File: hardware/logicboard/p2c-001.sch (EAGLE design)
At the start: 47 parts, among them IC1 74LS07N, K1 G5V1, T1 2SC1815

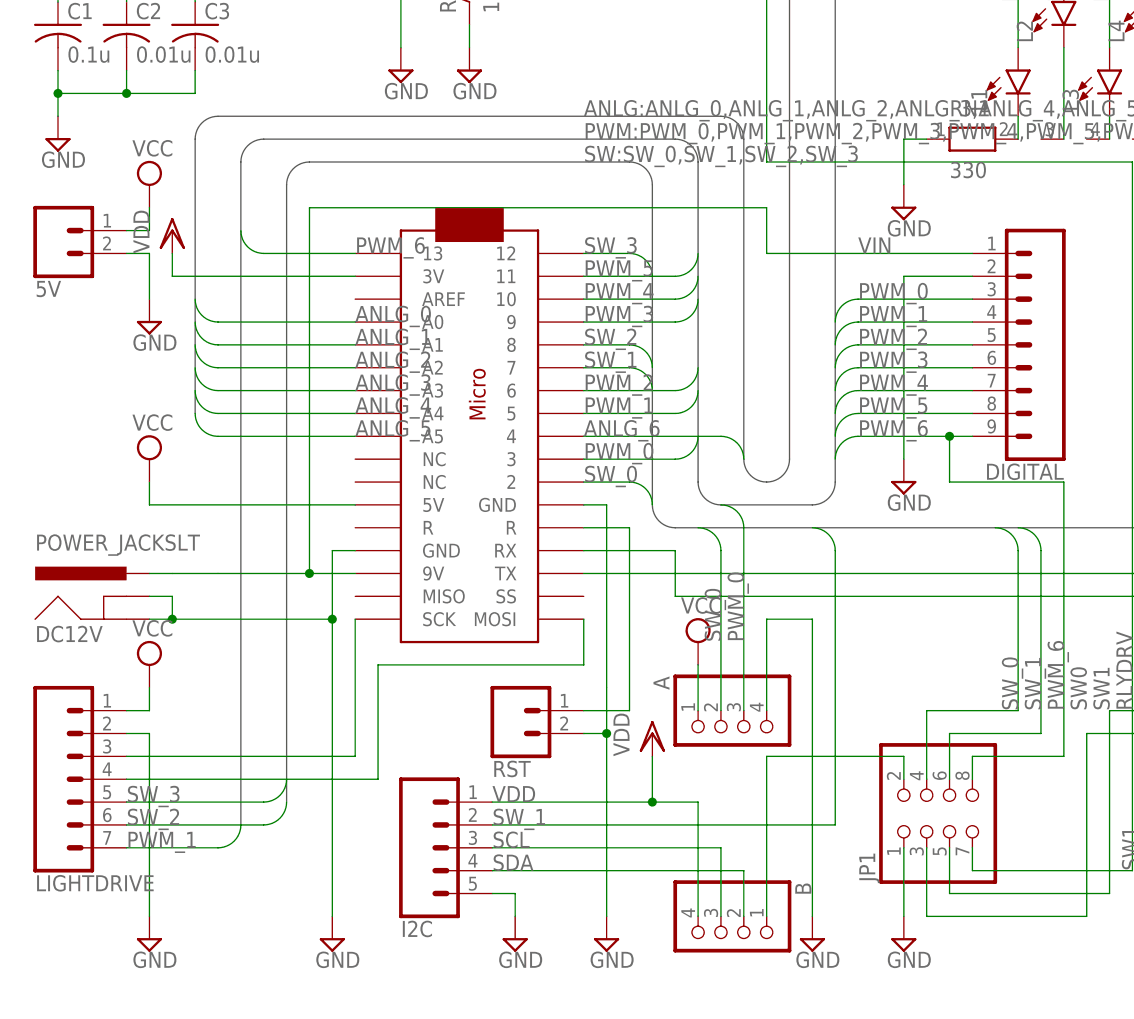
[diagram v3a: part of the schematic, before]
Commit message: Reversed Digital pin.
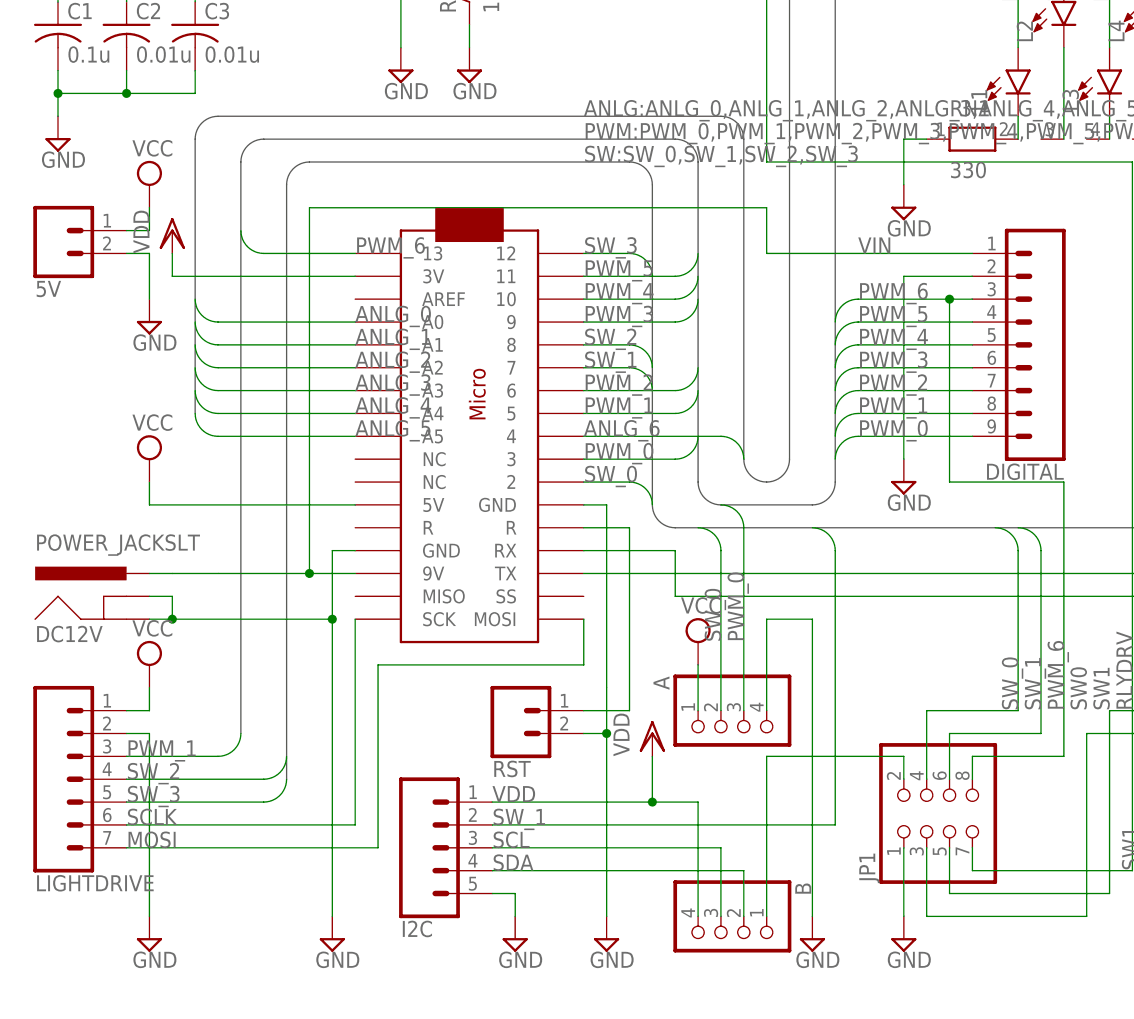
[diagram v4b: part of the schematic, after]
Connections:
- removed net SCK: LIGHTDRIVE.3, U$2.SCK
- new net SCLK: LIGHTDRIVE.6, U$2.SCK
- net MOSI: now also LIGHTDRIVE.7; no longer LIGHTDRIVE.4
- net PWM_0: now also DIGITAL.9; no longer DIGITAL.3
- net PWM_1: now also DIGITAL.8, LIGHTDRIVE.3; no longer DIGITAL.4, LIGHTDRIVE.7
- net PWM_2: now also DIGITAL.7; no longer DIGITAL.5
- net PWM_4: now also DIGITAL.5; no longer DIGITAL.7
- net PWM_5: now also DIGITAL.4; no longer DIGITAL.8
- net PWM_6: now also DIGITAL.3; no longer DIGITAL.9
- net SW_2: now also LIGHTDRIVE.4; no longer LIGHTDRIVE.6
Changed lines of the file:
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@@
 <setting verticaltext="up"/>
 </settings>
-<grid distance="0.1" unitdist="inch" unit="inch" style="lines" multiple="1" display="no" altdistance="0.01" altunitdist="inch" altunit="inch"/>
+<grid distance="0.1" unitdist="inch" unit="inch" style="dots" multiple="1" display="yes" altdistance="0.01" altunitdist="inch" altunit="inch"/>
 <layers>
 <layer number="1" name="Top" color="4" fill="1" visible="no" active="no"/>
@@
 <bus name="PWM:PWM_0,PWM_1,PWM_2,PWM_3,PWM_4,PWM_5,PWM_6">
 <segment>
-<wire x1="30.48" y1="27.94" x2="30.48" y2="101.6" width="0.762" layer="92"/>
+<wire x1="30.48" y1="38.1" x2="30.48" y2="101.6" width="0.762" layer="92"/>
 <wire x1="30.48" y1="101.6" x2="33.02" y2="104.14" width="0.762" layer="92" curve="-90"/>
 <wire x1="33.02" y1="104.14" x2="78.74" y2="104.14" width="0.762" layer="92"/>
@@
 <wire x1="73.66" y1="101.6" x2="38.1" y2="101.6" width="0.762" layer="92"/>
 <wire x1="38.1" y1="101.6" x2="35.56" y2="99.06" width="0.762" layer="92" curve="90"/>
-<wire x1="35.56" y1="99.06" x2="35.56" y2="30.48" width="0.762" layer="92"/>
+<wire x1="35.56" y1="99.06" x2="35.56" y2="33.02" width="0.762" layer="92"/>
 <label x="68.58" y="101.6" size="1.778" layer="95"/>
 </segment>
@@
 </segment>
 <segment>
-<pinref part="LIGHTDRIVE" gate="G$1" pin="6"/>
-<wire x1="35.56" y1="30.48" x2="33.02" y2="27.94" width="0.1524" layer="91" curve="-90"/>
-<wire x1="33.02" y1="27.94" x2="17.78" y2="27.94" width="0.1524" layer="91"/>
-<label x="17.78" y="27.94" size="1.778" layer="95"/>
+<pinref part="LIGHTDRIVE" gate="G$1" pin="4"/>
+<wire x1="35.56" y1="35.56" x2="33.02" y2="33.02" width="0.1524" layer="91" curve="-90"/>
+<wire x1="33.02" y1="33.02" x2="17.78" y2="33.02" width="0.1524" layer="91"/>
+<label x="17.78" y="33.02" size="1.778" layer="95"/>
 </segment>
 </net>
@@
 </segment>
 <segment>
-<wire x1="96.52" y1="68.58" x2="99.06" y2="71.12" width="0.1524" layer="91" curve="-90"/>
-<wire x1="99.06" y1="71.12" x2="109.22" y2="71.12" width="0.1524" layer="91"/>
-<label x="99.06" y="71.12" size="1.778" layer="95"/>
-<wire x1="109.22" y1="71.12" x2="111.76" y2="71.12" width="0.1524" layer="91"/>
-<wire x1="109.22" y1="71.12" x2="109.22" y2="66.04" width="0.1524" layer="91"/>
-<junction x="109.22" y="71.12"/>
+<pinref part="DIGITAL" gate="G$1" pin="3"/>
+<wire x1="96.52" y1="83.82" x2="99.06" y2="86.36" width="0.1524" layer="91" curve="-90"/>
+<wire x1="99.06" y1="86.36" x2="109.22" y2="86.36" width="0.1524" layer="91"/>
+<label x="99.06" y="86.36" size="1.778" layer="95"/>
+<wire x1="109.22" y1="86.36" x2="111.76" y2="86.36" width="0.1524" layer="91"/>
 <wire x1="109.22" y1="66.04" x2="121.92" y2="66.04" width="0.1524" layer="91"/>
 <wire x1="121.92" y1="66.04" x2="121.92" y2="35.56" width="0.1524" layer="91"/>
@@
 <wire x1="111.76" y1="35.56" x2="111.76" y2="33.02" width="0.1524" layer="91"/>
 <label x="121.92" y="40.64" size="1.778" layer="95" rot="R90"/>
-<pinref part="DIGITAL" gate="G$1" pin="9"/>
+<wire x1="109.22" y1="86.36" x2="109.22" y2="66.04" width="0.1524" layer="91"/>
+<junction x="109.22" y="86.36"/>
 </segment>
 </net>
@@
 </segment>
 <segment>
-<wire x1="96.52" y1="71.12" x2="99.06" y2="73.66" width="0.1524" layer="91" curve="-90"/>
-<wire x1="99.06" y1="73.66" x2="111.76" y2="73.66" width="0.1524" layer="91"/>
-<label x="99.06" y="73.66" size="1.778" layer="95"/>
-<pinref part="DIGITAL" gate="G$1" pin="8"/>
+<pinref part="DIGITAL" gate="G$1" pin="4"/>
+<wire x1="96.52" y1="81.28" x2="99.06" y2="83.82" width="0.1524" layer="91" curve="-90"/>
+<wire x1="99.06" y1="83.82" x2="111.76" y2="83.82" width="0.1524" layer="91"/>
+<label x="99.06" y="83.82" size="1.778" layer="95"/>
 </segment>
 </net>
@@
 </segment>
 <segment>
-<wire x1="96.52" y1="73.66" x2="99.06" y2="76.2" width="0.1524" layer="91" curve="-90"/>
-<wire x1="99.06" y1="76.2" x2="111.76" y2="76.2" width="0.1524" layer="91"/>
-<label x="99.06" y="76.2" size="1.778" layer="95"/>
-<pinref part="DIGITAL" gate="G$1" pin="7"/>
+<pinref part="DIGITAL" gate="G$1" pin="5"/>
+<wire x1="96.52" y1="78.74" x2="99.06" y2="81.28" width="0.1524" layer="91" curve="-90"/>
+<wire x1="99.06" y1="81.28" x2="111.76" y2="81.28" width="0.1524" layer="91"/>
+<label x="99.06" y="81.28" size="1.778" layer="95"/>
 </segment>
 </net>
@@
 </segment>
 <segment>
+<pinref part="DIGITAL" gate="G$1" pin="6"/>
 <wire x1="96.52" y1="76.2" x2="99.06" y2="78.74" width="0.1524" layer="91" curve="-90"/>
 <wire x1="99.06" y1="78.74" x2="111.76" y2="78.74" width="0.1524" layer="91"/>
 <label x="99.06" y="78.74" size="1.778" layer="95"/>
-<pinref part="DIGITAL" gate="G$1" pin="6"/>
 </segment>
 </net>
@@
 </segment>
 <segment>
-<wire x1="96.52" y1="83.82" x2="99.06" y2="86.36" width="0.1524" layer="91" curve="-90"/>
-<wire x1="99.06" y1="86.36" x2="111.76" y2="86.36" width="0.1524" layer="91"/>
-<label x="99.06" y="86.36" size="1.778" layer="95"/>
-<pinref part="DIGITAL" gate="G$1" pin="3"/>
-</segment>
-<segment>
 <pinref part="A" gate="A" pin="3"/>
 <wire x1="83.82" y1="63.5" x2="86.36" y2="60.96" width="0.1524" layer="91" curve="-90"/>
@@
 <label x="86.36" y="48.26" size="1.778" layer="95" rot="R90"/>
 </segment>
+<segment>
+<pinref part="DIGITAL" gate="G$1" pin="9"/>
+<wire x1="96.52" y1="68.58" x2="99.06" y2="71.12" width="0.1524" layer="91" curve="-90"/>
+<wire x1="99.06" y1="71.12" x2="111.76" y2="71.12" width="0.1524" layer="91"/>
+<label x="99.06" y="71.12" size="1.778" layer="95"/>
+</segment>
 </net>
 <net name="PWM_2" class="0">
@@
 </segment>
 <segment>
-<wire x1="96.52" y1="78.74" x2="99.06" y2="81.28" width="0.1524" layer="91" curve="-90"/>
-<wire x1="99.06" y1="81.28" x2="111.76" y2="81.28" width="0.1524" layer="91"/>
-<label x="99.06" y="81.28" size="1.778" layer="95"/>
-<pinref part="DIGITAL" gate="G$1" pin="5"/>
+<pinref part="DIGITAL" gate="G$1" pin="7"/>
+<wire x1="96.52" y1="73.66" x2="99.06" y2="76.2" width="0.1524" layer="91" curve="-90"/>
+<wire x1="99.06" y1="76.2" x2="111.76" y2="76.2" width="0.1524" layer="91"/>
+<label x="99.06" y="76.2" size="1.778" layer="95"/>
 </segment>
 </net>
@@
 </segment>
 <segment>
-<wire x1="96.52" y1="81.28" x2="99.06" y2="83.82" width="0.1524" layer="91" curve="-90"/>
-<wire x1="99.06" y1="83.82" x2="111.76" y2="83.82" width="0.1524" layer="91"/>
-<label x="99.06" y="83.82" size="1.778" layer="95"/>
-<pinref part="DIGITAL" gate="G$1" pin="4"/>
-</segment>
-<segment>
-<pinref part="LIGHTDRIVE" gate="G$1" pin="7"/>
-<wire x1="30.48" y1="27.94" x2="27.94" y2="25.4" width="0.1524" layer="91" curve="-90"/>
-<wire x1="27.94" y1="25.4" x2="17.78" y2="25.4" width="0.1524" layer="91"/>
-<label x="17.78" y="25.4" size="1.778" layer="95"/>
+<pinref part="LIGHTDRIVE" gate="G$1" pin="3"/>
+<wire x1="30.48" y1="38.1" x2="27.94" y2="35.56" width="0.1524" layer="91" curve="-90"/>
+<wire x1="27.94" y1="35.56" x2="17.78" y2="35.56" width="0.1524" layer="91"/>
+<label x="17.78" y="35.56" size="1.778" layer="95"/>
+</segment>
+<segment>
+<pinref part="DIGITAL" gate="G$1" pin="8"/>
+<wire x1="96.52" y1="71.12" x2="99.06" y2="73.66" width="0.1524" layer="91" curve="-90"/>
+<wire x1="99.06" y1="73.66" x2="111.76" y2="73.66" width="0.1524" layer="91"/>
+<label x="99.06" y="73.66" size="1.778" layer="95"/>
 </segment>
 </net>
@@
 </segment>
 </net>
-<net name="SCK" class="0">
-<segment>
-<pinref part="U$2" gate="G$1" pin="SCK"/>
-<wire x1="43.18" y1="50.8" x2="43.18" y2="35.56" width="0.1524" layer="91"/>
-<pinref part="LIGHTDRIVE" gate="G$1" pin="3"/>
-<wire x1="43.18" y1="35.56" x2="17.78" y2="35.56" width="0.1524" layer="91"/>
-</segment>
-</net>
 <net name="MOSI" class="0">
 <segment>
@@
 <wire x1="68.58" y1="50.8" x2="68.58" y2="45.72" width="0.1524" layer="91"/>
 <wire x1="68.58" y1="45.72" x2="45.72" y2="45.72" width="0.1524" layer="91"/>
-<wire x1="45.72" y1="45.72" x2="45.72" y2="33.02" width="0.1524" layer="91"/>
-<pinref part="LIGHTDRIVE" gate="G$1" pin="4"/>
-<wire x1="45.72" y1="33.02" x2="17.78" y2="33.02" width="0.1524" layer="91"/>
-</segment>
-</net>
+<wire x1="45.72" y1="45.72" x2="45.72" y2="25.4" width="0.1524" layer="91"/>
+<pinref part="LIGHTDRIVE" gate="G$1" pin="7"/>
+<wire x1="45.72" y1="25.4" x2="17.78" y2="25.4" width="0.1524" layer="91"/>
+<label x="17.78" y="25.4" size="1.778" layer="95"/>
+</segment>
+</net>
+<net name="SCLK" class="0">
+<segment>
+<pinref part="U$2" gate="G$1" pin="SCK"/>
+<wire x1="43.18" y1="50.8" x2="43.18" y2="27.94" width="0.1524" layer="91"/>
+<pinref part="LIGHTDRIVE" gate="G$1" pin="6"/>
+<wire x1="43.18" y1="27.94" x2="17.78" y2="27.94" width="0.1524" layer="91"/>
+<label x="17.78" y="27.94" size="1.778" layer="95"/>
+</segment>
+</net>

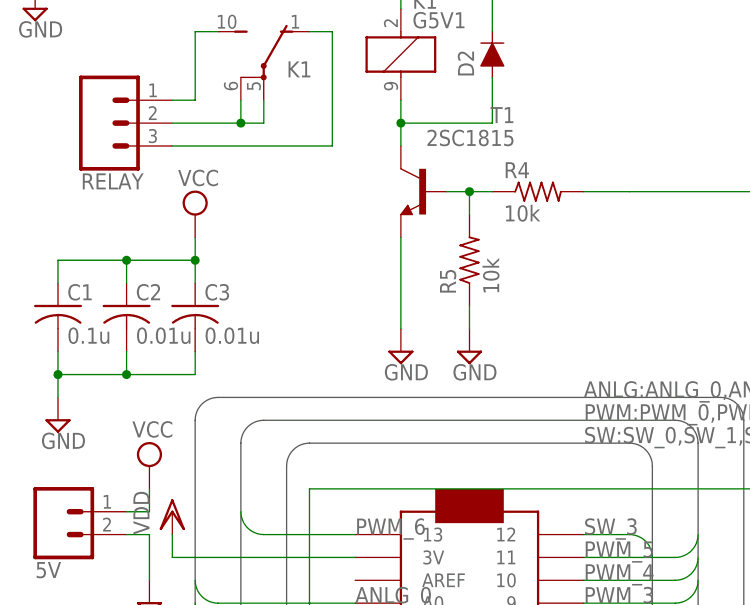
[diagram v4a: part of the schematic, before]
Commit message: Added I2C Rs.
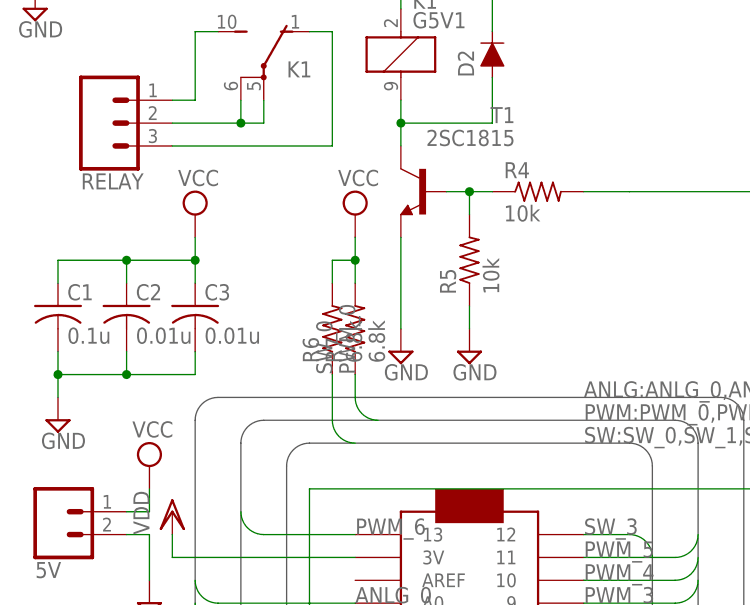
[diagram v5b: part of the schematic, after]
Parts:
- added R6, R7: 6.8k, resistor:R-US_0204/5
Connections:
- net PWM_0: now also R7.1
- net SW_0: now also R6.1
- net VCC: now also R6.2, R7.2
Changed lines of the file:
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@@
 <setting verticaltext="up"/>
 </settings>
-<grid distance="0.1" unitdist="inch" unit="inch" style="dots" multiple="1" display="yes" altdistance="0.01" altunitdist="inch" altunit="inch"/>
+<grid distance="0.1" unitdist="inch" unit="inch" style="lines" multiple="1" display="no" altdistance="0.01" altunitdist="inch" altunit="inch"/>
 <layers>
 <layer number="1" name="Top" color="4" fill="1" visible="no" active="no"/>
@@
 <part name="POGOPIN" library="pinhead" library_urn="urn:adsk.eagle:library:325" deviceset="PINHD-1X1" device="" package3d_urn="urn:adsk.eagle:package:22485/2"/>
 <part name="5V" library="SparkFun-Connectors" library_urn="urn:adsk.eagle:library:513" deviceset="CONN_02" device="" package3d_urn="urn:adsk.eagle:package:38039/1"/>
+<part name="SUPPLY26" library="supply2" library_urn="urn:adsk.eagle:library:372" deviceset="VCC" device=""/>
+<part name="R6" library="resistor" library_urn="urn:adsk.eagle:library:348" deviceset="R-US_" device="0204/5" package3d_urn="urn:adsk.eagle:package:25955/1" value="6.8k"/>
+<part name="R7" library="resistor" library_urn="urn:adsk.eagle:library:348" deviceset="R-US_" device="0204/5" package3d_urn="urn:adsk.eagle:package:25955/1" value="6.8k"/>
 </parts>
 <sheets>
@@
 <instance part="POGOPIN" gate="G$1" x="236.22" y="127"/>
 <instance part="5V" gate="G$1" x="10.16" y="93.98" rot="MR180"/>
+<instance part="SUPPLY26" gate="G$1" x="43.18" y="127"/>
+<instance part="R6" gate="G$1" x="40.64" y="114.3" rot="R90"/>
+<instance part="R7" gate="G$1" x="43.18" y="114.3" rot="R90"/>
 </instances>
 <busses>
@@
 <wire x1="20.32" y1="40.64" x2="17.78" y2="40.64" width="0.1524" layer="91"/>
 </segment>
+<segment>
+<pinref part="R6" gate="G$1" pin="2"/>
+<wire x1="40.64" y1="119.38" x2="40.64" y2="121.92" width="0.1524" layer="91"/>
+<wire x1="40.64" y1="121.92" x2="43.18" y2="121.92" width="0.1524" layer="91"/>
+<pinref part="R7" gate="G$1" pin="2"/>
+<wire x1="43.18" y1="121.92" x2="43.18" y2="119.38" width="0.1524" layer="91"/>
+<pinref part="SUPPLY26" gate="G$1" pin="VCC"/>
+<wire x1="43.18" y1="121.92" x2="43.18" y2="124.46" width="0.1524" layer="91"/>
+<junction x="43.18" y="121.92"/>
+</segment>
 </net>
 <net name="MIDIOUT-" class="0">
@@
 <label x="83.82" y="48.26" size="1.778" layer="95" rot="R90"/>
 </segment>
+<segment>
+<wire x1="43.18" y1="101.6" x2="40.64" y2="104.14" width="0.1524" layer="91" curve="-90"/>
+<wire x1="40.64" y1="104.14" x2="40.64" y2="109.22" width="0.1524" layer="91"/>
+<label x="40.64" y="109.22" size="1.778" layer="95" rot="R90"/>
+<pinref part="R6" gate="G$1" pin="1"/>
+</segment>
 </net>
 <net name="LED1K" class="0">
@@
 <label x="99.06" y="71.12" size="1.778" layer="95"/>
 </segment>
-</net>
+<segment>
+<wire x1="45.72" y1="104.14" x2="43.18" y2="106.68" width="0.1524" layer="91" curve="-90"/>
+<wire x1="43.18" y1="106.68" x2="43.18" y2="109.22" width="0.1524" layer="91"/>
+<label x="43.18" y="109.22" size="1.778" layer="95" rot="R90"/>
+<pinref part="R7" gate="G$1" pin="1"/>
+</segment>
+</net>

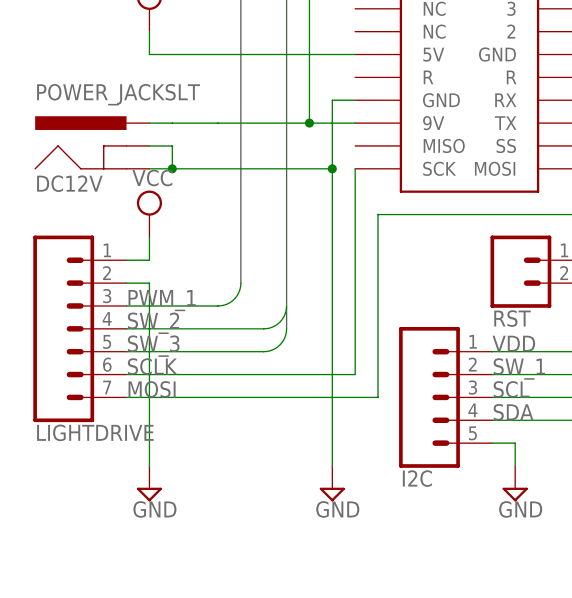
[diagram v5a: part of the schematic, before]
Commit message: Swapped Vcc and GND of LD.
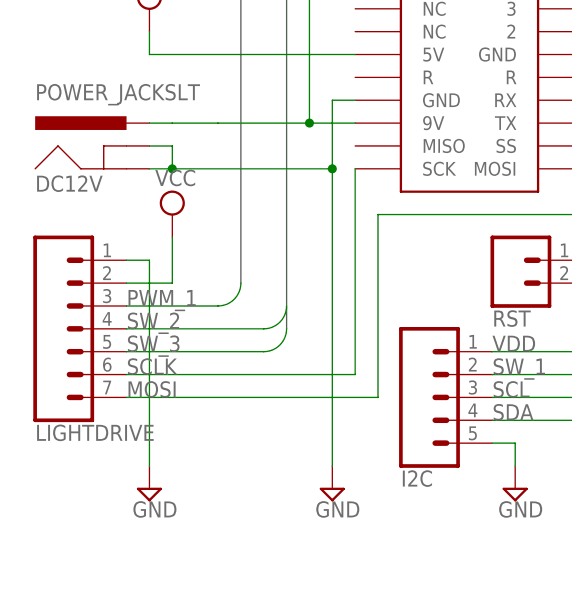
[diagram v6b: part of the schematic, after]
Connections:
- net GND: now also LIGHTDRIVE.1; no longer LIGHTDRIVE.2
- net VCC: now also LIGHTDRIVE.2; no longer LIGHTDRIVE.1
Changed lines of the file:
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@@
 <instance part="RCV" gate="G$1" x="144.78" y="99.06" rot="R90"/>
 <instance part="LIGHTDRIVE" gate="G$1" x="12.7" y="35.56" rot="MR180"/>
-<instance part="SUPPLY12" gate="G$1" x="20.32" y="45.72"/>
+<instance part="SUPPLY12" gate="G$1" x="22.86" y="45.72"/>
 <instance part="I2C" gate="G$1" x="50.8" y="25.4" rot="MR180"/>
 <instance part="SUPPLY25" gate="GND" x="60.96" y="15.24"/>
@@
 </segment>
 <segment>
-<pinref part="LIGHTDRIVE" gate="G$1" pin="2"/>
 <pinref part="SUPPLY13" gate="GND" pin="GND"/>
-<wire x1="17.78" y1="38.1" x2="20.32" y2="38.1" width="0.1524" layer="91"/>
-<wire x1="20.32" y1="38.1" x2="20.32" y2="17.78" width="0.1524" layer="91"/>
+<wire x1="20.32" y1="40.64" x2="20.32" y2="17.78" width="0.1524" layer="91"/>
+<pinref part="LIGHTDRIVE" gate="G$1" pin="1"/>
+<wire x1="20.32" y1="40.64" x2="17.78" y2="40.64" width="0.1524" layer="91"/>
 </segment>
 <segment>
@@
 </segment>
 <segment>
-<pinref part="SUPPLY12" gate="G$1" pin="VCC"/>
-<wire x1="20.32" y1="43.18" x2="20.32" y2="40.64" width="0.1524" layer="91"/>
-<pinref part="LIGHTDRIVE" gate="G$1" pin="1"/>
-<wire x1="20.32" y1="40.64" x2="17.78" y2="40.64" width="0.1524" layer="91"/>
-</segment>
-<segment>
 <pinref part="R6" gate="G$1" pin="2"/>
 <wire x1="40.64" y1="119.38" x2="40.64" y2="121.92" width="0.1524" layer="91"/>
@@
 <junction x="43.18" y="121.92"/>
 </segment>
-</net>
+<segment>
+<pinref part="SUPPLY12" gate="G$1" pin="VCC"/>
+<wire x1="22.86" y1="43.18" x2="22.86" y2="38.1" width="0.1524" layer="91"/>
+<pinref part="LIGHTDRIVE" gate="G$1" pin="2"/>
+<wire x1="22.86" y1="38.1" x2="17.78" y2="38.1" width="0.1524" layer="91"/>
+</segment>
+</net>
